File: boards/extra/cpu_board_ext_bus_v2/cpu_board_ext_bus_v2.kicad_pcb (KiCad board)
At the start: 2 copper layers, 95.2 x 95.2 mm, 43 parts, among them J1 Exp. Conn. A, J2 Exp. Conn. B, J3 Power, J4 Exp. Conn. C, J5 EXT_CLK, J6 CPU_CLK_SEL, J7 BUS_CLK_SEL, U1 Z80CPPLC44, U2 GAL16V8, U3 74LS244, U4 74LS244, U5 74LS245, U6 74LS244, U7 74LS30, U8 ATF1502AS-7JX44, X1 INT_CLK

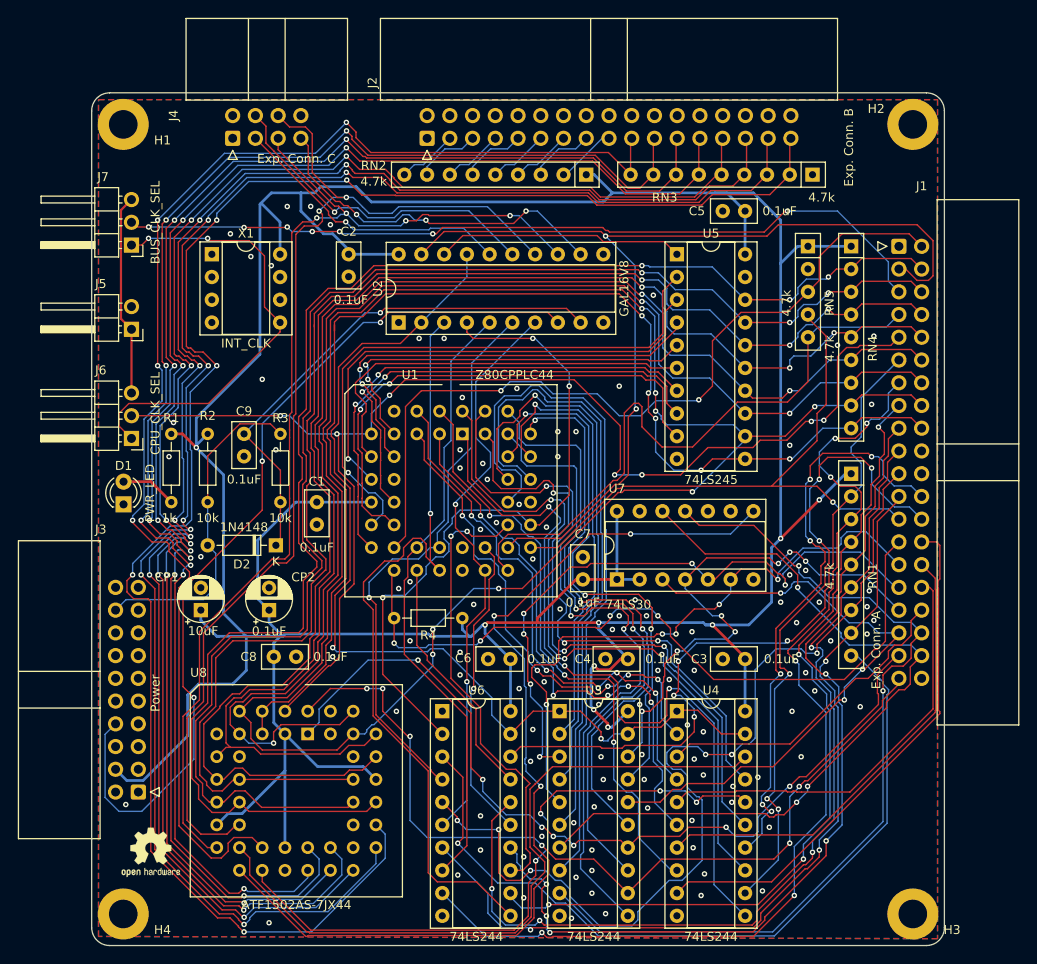
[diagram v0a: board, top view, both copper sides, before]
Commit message: Extended CPU board update
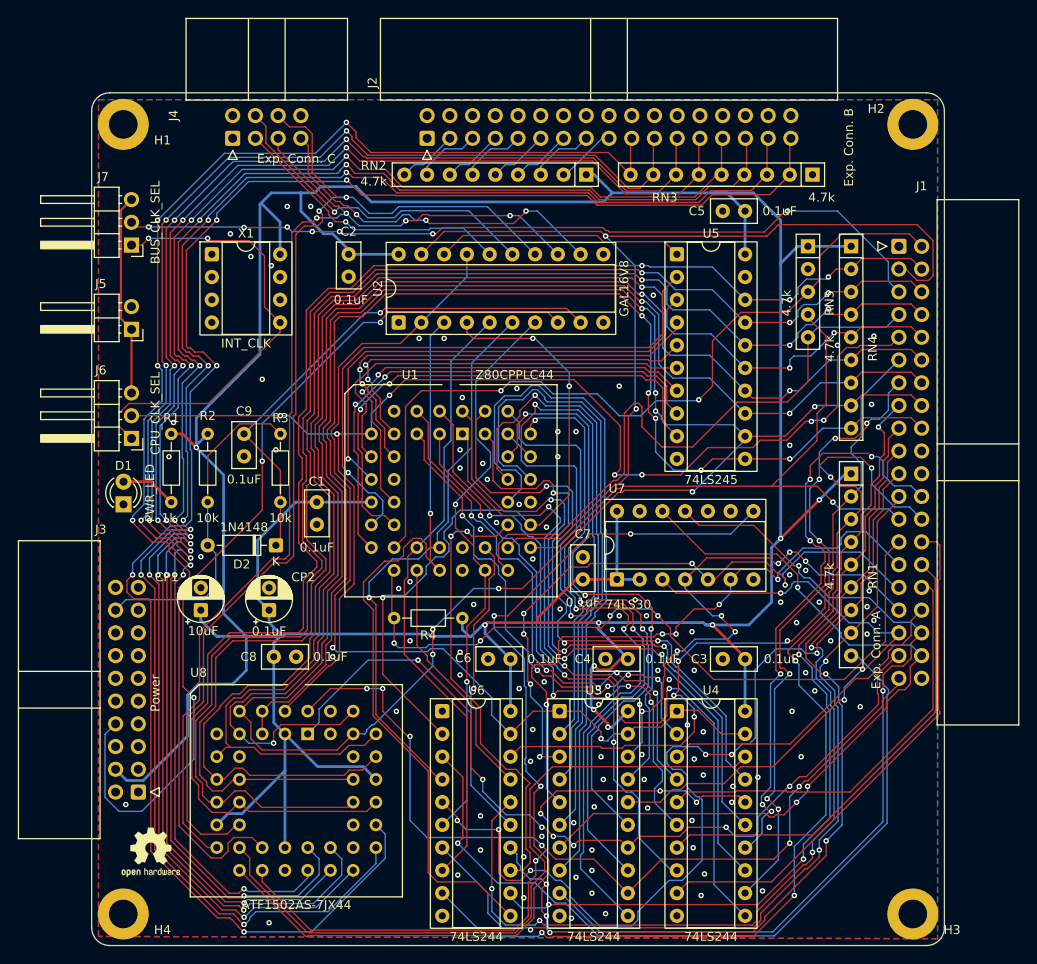
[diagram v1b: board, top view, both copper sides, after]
